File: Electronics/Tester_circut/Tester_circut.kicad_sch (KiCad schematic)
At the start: 5 parts, among them Q1 BC547

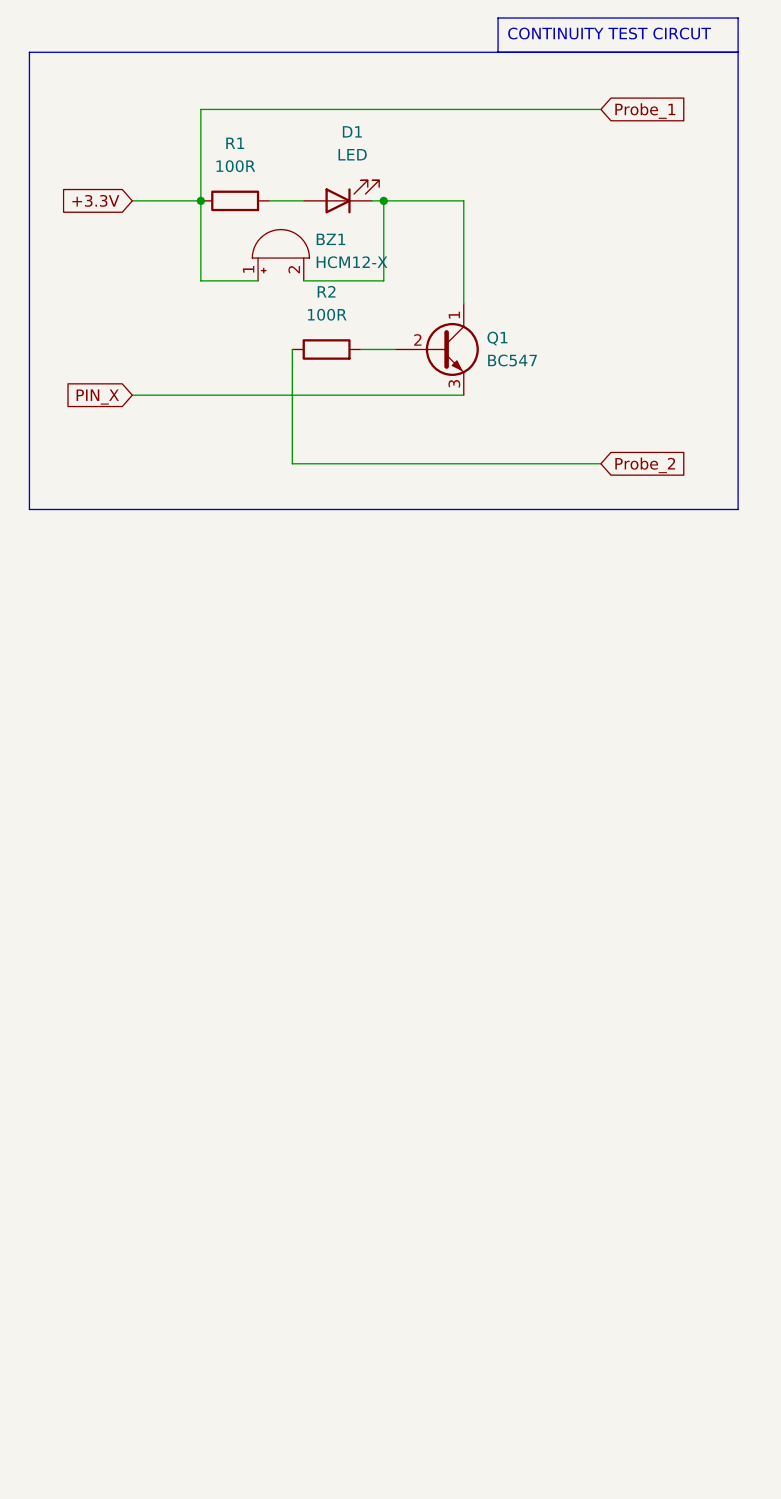
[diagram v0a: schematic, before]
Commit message: Electronics update
Schematic for the end stop sensors added
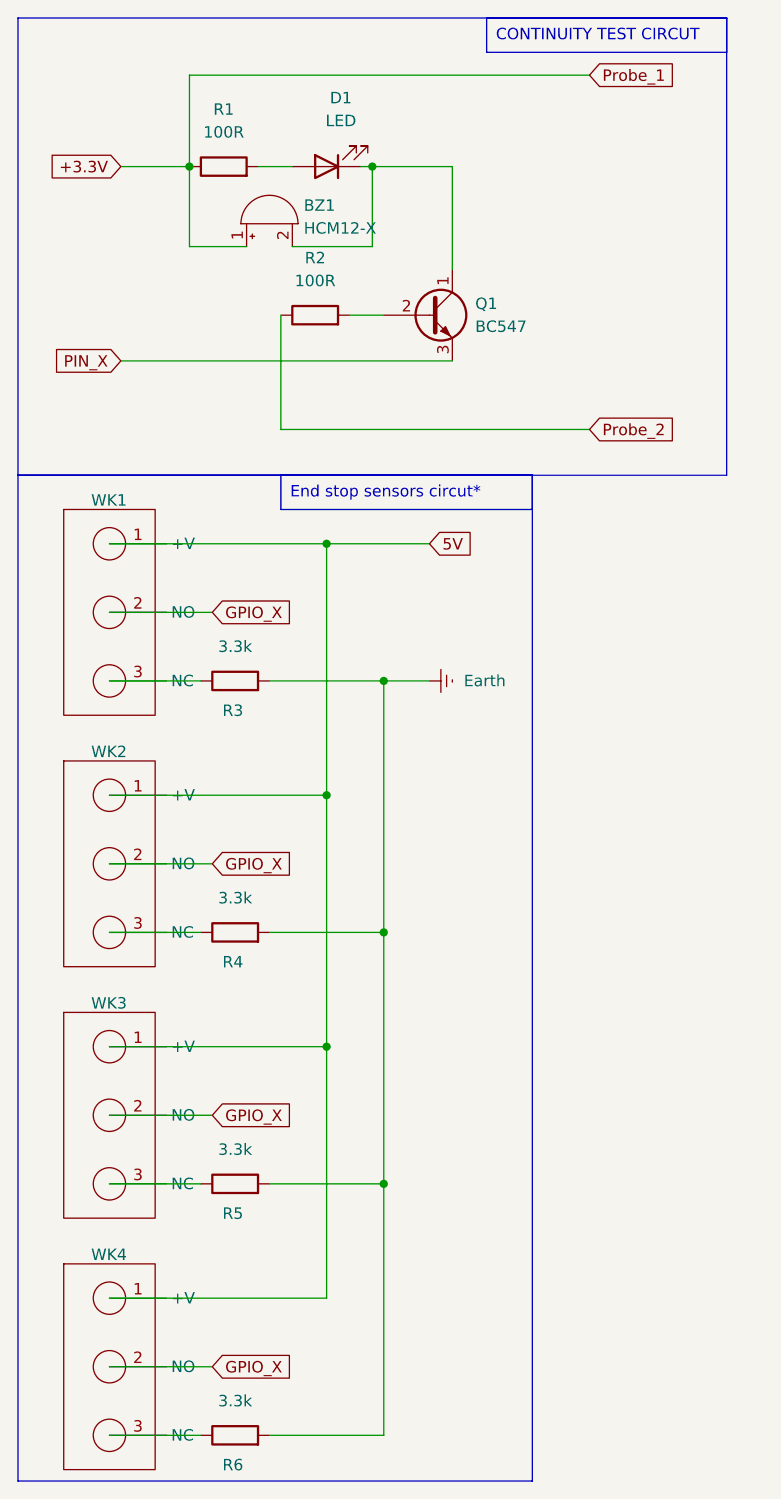
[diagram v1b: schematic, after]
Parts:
- added R3, R4, R5, R6: 3.3k, symbol Device:R
- added WK1, WK2, WK3, WK4: ~, symbol Sensor:End_stop_mechanical_sensor
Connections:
- new net: R5.1, WK3.3 (NC)
- new net: R6.1, WK4.3 (NC)
- new net: R4.1, WK2.3 (NC)
- new net: R3.1, WK1.3 (NC)
- new net 5V: WK1.1 (+V), WK2.1 (+V), WK3.1 (+V), WK4.1 (+V)
- new net Earth: R3.2, R4.2, R5.2, R6.2
- new net GPIO_X: WK1.2 (NO), WK2.2 (NO), WK3.2 (NO), WK4.2 (NO)
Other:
- moved on the sheet: BZ1, D1, Q1, R1, R2

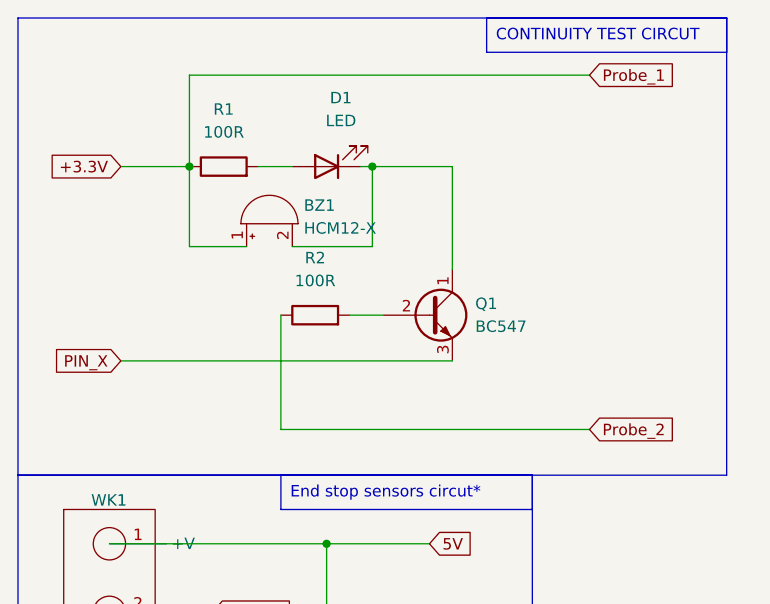
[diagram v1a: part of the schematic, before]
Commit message: Tester circut update
Fixed testing circut based on software requirements
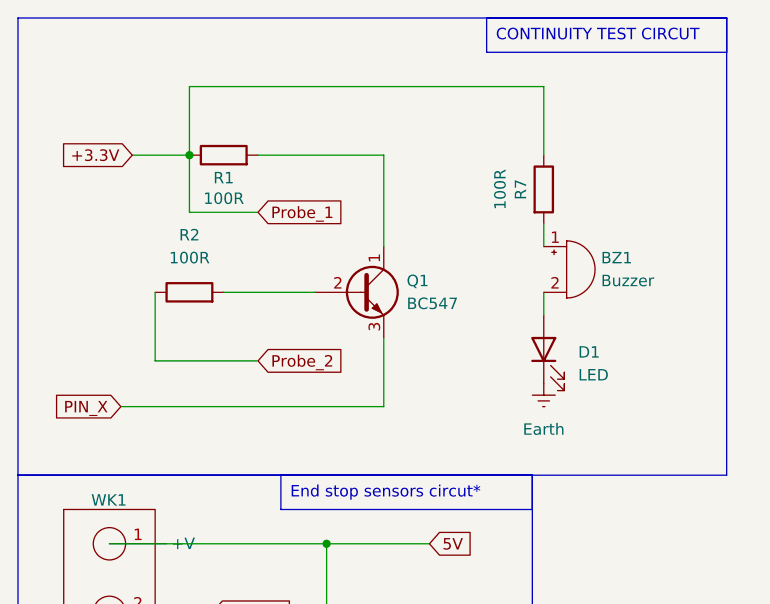
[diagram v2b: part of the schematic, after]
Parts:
- added R7: 100R, symbol Device:R
- BZ1: value HCM12-X -> Buzzer
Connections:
- net +3.3V: now also R7.1; no longer BZ1.1 (+)
- net Earth: now also D1.1 (K)
- net at R1.2: now also Q1.1 (C); no longer D1.2 (A)
- new net: BZ1.1 (+), R7.2
- new net: BZ1.2 (-), D1.2 (A)
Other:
- moved on the sheet: Q1, R1, R2

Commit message: PCB and schematics update
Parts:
- removed BZ1: Buzzer, symbol Device:Buzzer
- removed D1: LED, symbol Device:LED
- removed Q1: BC547, Package_TO_SOT_THT:TO-92_Inline, symbol Transistor_BJT:BC547
- removed R1, R2, R7: 100R, symbol Device:R
- removed R3, R4, R5, R6: 3.3k, symbol Device:R
- removed WK1, WK2, WK3, WK4: ~, symbol Sensor:End_stop_mechanical_sensor
- added A1: NUCLEO-F746ZG, NUCLEO-F746ZG:MODULE_NUCLEO-F746ZG, symbol NUCLEO-F746ZG:NUCLEO-F746ZG
- added J11, J12: KF301-2P, KF301-2P:HANDSON_KF301-2P, symbol KF301-2P:KF301-2P
- added SW1: Encoder, Library:encoder, symbol Device:RotaryEncoder_Switch
- added SW2: SW_DPST_x2, symbol Switch:SW_DPST_x2
- added U1: LF90_TO220, Package_TO_SOT_THT:TO-220-3_Vertical, symbol Regulator_Linear:LF90_TO220
- added U4: LCD, Library:LCD, symbol TMC2209_SILENTSTEPSTICK:LCD
- added U7: LM7805_TO220, Package_TO_SOT_THT:TO-220-3_Vertical, symbol Regulator_Linear:LM7805_TO220
- added U8: LF33_TO220, Package_TO_SOT_THT:TO-220-3_Vertical, symbol Regulator_Linear:LF33_TO220
- added U9: Power_supply, Library:POWER_SUPPLY, symbol Converter_ACDC:U
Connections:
- new net: SW2.4 (B), U9.2 (N)
- new net: J11.2, U1.1 (VI), U7.1 (VI)
- new net: SW2.2 (B), U9.1 (L)
- new net BtnCtr: A1.CN10_6 (D5/TIMER_A_PWM2)
- new net BtnDown: A1.CN10_12 (D2/IO)
- new net BtnLeft: A1.CN9_29 (D65/IO)
- new net BtnRight: A1.CN9_30 (D64/IO)
- new net BtnUp: A1.CN10_8 (D4/IO)
- new net ENC_CLK: A1.CN10_19 (D28/QSPI_BK1_IO3), SW1.A
- new net ENC_DT: A1.CN10_21 (D29/QSPI_BK1_IO1), SW1.B
- new net EncoderBtn: A1.CN10_7 (A6/ADC_A_IN), SW1.C
- new net End stop sensors/+5V: SW1.S1, U4.2 (VCC), U7.3 (VO), U8.1 (VI)
- new net EndStop1: A1.CN9_14 (D56/SAI_A_MCLK)
- new net EndStop2: A1.CN9_16 (D57/SAI_A_FS)
- new net EndStop3: A1.CN7_17 (D24/SPI_B_NSS)
- new net EndStop4: A1.CN7_15 (D23/I2S_B_CK/SPI_B_SCK)
- new net Fans/+3.3V: U8.3 (VO)
- new net GND: A1.CN10_17 (GND_CN10), A1.CN10_22 (GND_CN10), A1.CN10_27 (GND_CN10), A1.CN10_5 (GND_CN10), A1.CN7_8 (GND_CN7), A1.CN8_11 (GND_CN8), A1.CN8_13 (GND_CN8), A1.CN9_12 (GND_CN9), A1.CN9_23 (GND_CN9), J11.1, SW1.S2, U1.2 (GND), U4.1 (GND), U7.2 (GND), U8.2 (GND)
- new net I2C1_SCL: A1.CN10_13 (D26/QSPI_CS), U4.4 (SCL)
- new net I2C1_SDA: A1.CN7_4 (D14/I2C_A_SDA), U4.3 (SDA)
- new net Motor drivers/GND: J12.1
- new net Motor drivers/Motor_+12V: J12.2
- new net SPI2_CLK: A1.CN9_10 (D55/USART_B_CTS)
- new net SPI2_MISO: A1.CN10_9 (A7/ADC_B_IN)
- new net SPI2_MOSI: A1.CN9_5 (A2/ADC123_IN13)
- new net SPI_cs: A1.CN7_16 (D10/SPI_A_CS/TIM_B_PWM3)
- new net Servo1PWM: A1.CN9_28 (D63/SAI_B_FS)
- new net Servo2PWM: A1.CN10_29 (D32/TIMER_C_PWM1)
- new net Test_pin: A1.CN9_1 (A0/ADC123_IN3)
- new net USART2_RX: A1.CN9_4 (D52/USART_B_RX)
- new net USART2_TX: A1.CN9_6 (D53/USART_B_TX)
- new net VIN_STM: A1.CN8_15 (VIN_CN8), U1.3 (VO)
- new net Wall_+240V: SW2.1 (A)
- new net Wall_GND: SW2.3 (A)
- new net diag1: A1.CN7_18 (D9/TIMER_B_PWM2)
- new net diag2: A1.CN9_27 (D66/CAN_TX)
- new net diag3: A1.CN7_20 (D8/IO)
- new net diag4: A1.CN7_19 (D25/SPI_B_MISO)
- new net dir1: A1.CN9_26 (D62/SAI_B_MCLK)
- new net dir2: A1.CN7_13 (D22/I2S_B_SD/SPI_B_MOSI)
- new net dir3: A1.CN9_20 (D59/SAI_A_SD)
- new net dir4: A1.CN9_25 (D67/CAN_RX)
- new net enn1: A1.CN10_34 (D35/TIMER_C_PWM3)
- new net enn2: A1.CN7_9 (D20/I2S_B_WS)
- new net enn3: A1.CN9_22 (D60/SAI_B_SD)
- new net enn4: A1.CN9_21 (D68/I2C_B_SDA)
- new net step1: A1.CN10_32 (D36/TIMER_C_PWM2)
- new net step2: A1.CN7_11 (D21/I2S_B_MCK)
- new net step3: A1.CN9_18 (D58/SAI_A_SCK)
- new net step4: A1.CN7_2 (D15/I2C_A_SCL)
- no-connect marks 0 -> 50
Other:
- added sheet Buttons (buttons.kicad_sch)
- added sheet End stop sensors (endstop.kicad_sch)
- added sheet Fans (Fans.kicad_sch)
- added sheet Motor drivers (Motor_drivers.kicad_sch)
- added sheet Sd card reader (sdreader.kicad_sch)
- added sheet Servo motors (servo.kicad_sch)
- added sheet Tester circut (untitled.kicad_sch)
- title: (none) -> Flying probe tester - PCB shield for STM32F746ZG
